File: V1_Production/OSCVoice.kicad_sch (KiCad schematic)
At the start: 39 parts, among them U15 4066, U16 TL072, U22 SSI2131, U5 MCP6004, U8 4066

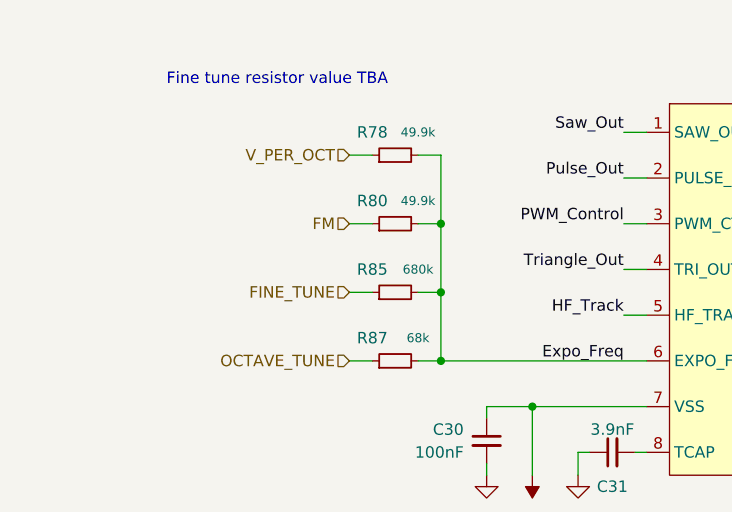
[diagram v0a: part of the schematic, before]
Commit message: Updates for v2 on control board
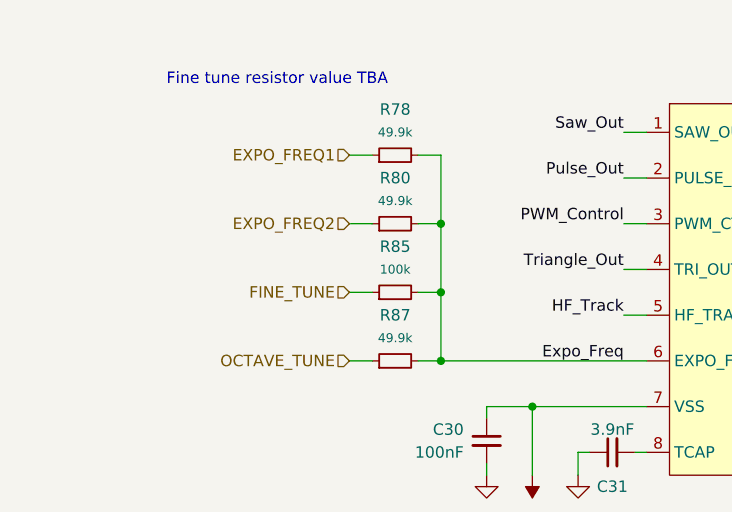
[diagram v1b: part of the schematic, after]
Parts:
- R85: value 680k -> 100k
- R87: value 68k -> 49.9k
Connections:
- net FM renamed EXPO_FREQ2
- net V_PER_OCT renamed EXPO_FREQ1
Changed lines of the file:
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@@
     (effects (font (size 0.3 0.3)) (justify right bottom))
   )
-  (hierarchical_label "FM" (shape input) (at 49.53 35.56 180)
+  (hierarchical_label "EXPO_FREQ2" (shape input) (at 49.53 35.56 180)
     (effects (font (size 1.27 1.27)) (justify right))
   )
@@
     (effects (font (size 1.27 1.27)) (justify right))
   )
-  (hierarchical_label "V_PER_OCT" (shape input) (at 49.53 27.94 180)
+  (hierarchical_label "EXPO_FREQ1" (shape input) (at 49.53 27.94 180)
     (effects (font (size 1.27 1.27)) (justify right))
   )
@@
   )
   (symbol (lib_id "Device:R_Small") (at 54.61 35.56 90) (unit 1)
-    (in_bom yes) (on_board yes)
-    (property "Reference" "R80" (id 0) (at 52.07 33.02 90))
-    (property "Value" "49.9k" (id 1) (at 57.15 33.02 90)
+    (in_bom yes) (on_board yes) (fields_autoplaced)
+    (property "Reference" "R80" (id 0) (at 54.61 30.48 90))
+    (property "Value" "49.9k" (id 1) (at 54.61 33.02 90)
       (effects (font (size 1 1)))
     )
@@
   )
   (symbol (lib_id "Device:R_Small") (at 54.61 50.8 90) (unit 1)
-    (in_bom yes) (on_board yes)
-    (property "Reference" "R87" (id 0) (at 52.07 48.26 90))
-    (property "Value" "68k" (id 1) (at 57.15 48.26 90)
+    (in_bom yes) (on_board yes) (fields_autoplaced)
+    (property "Reference" "R87" (id 0) (at 54.61 45.72 90))
+    (property "Value" "49.9k" (id 1) (at 54.61 48.26 90)
       (effects (font (size 1 1)))
     )
@@
   )
   (symbol (lib_id "Device:R_Small") (at 54.61 27.94 90) (unit 1)
-    (in_bom yes) (on_board yes)
-    (property "Reference" "R78" (id 0) (at 52.07 25.4 90))
-    (property "Value" "49.9k" (id 1) (at 57.15 25.4 90)
+    (in_bom yes) (on_board yes) (fields_autoplaced)
+    (property "Reference" "R78" (id 0) (at 54.61 22.86 90))
+    (property "Value" "49.9k" (id 1) (at 54.61 25.4 90)
       (effects (font (size 1 1)))
     )
@@
   )
   (symbol (lib_id "Device:R_Small") (at 54.61 43.18 90) (unit 1)
-    (in_bom yes) (on_board yes)
-    (property "Reference" "R85" (id 0) (at 52.07 40.64 90))
-    (property "Value" "680k" (id 1) (at 57.15 40.64 90)
+    (in_bom yes) (on_board yes) (fields_autoplaced)
+    (property "Reference" "R85" (id 0) (at 54.61 38.1 90))
+    (property "Value" "100k" (id 1) (at 54.61 40.64 90)
       (effects (font (size 1 1)))
     )
